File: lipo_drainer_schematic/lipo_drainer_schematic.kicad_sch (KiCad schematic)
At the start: 55 parts, among them J1 BATT, J2 FAN, J3 Vcal, J4 128x64_OLED, J5 Gcal, J6 Ical, Q1 MMBT3904, Q10 FQP27P06, Q11 FQP27P06, Q2 IRLML5103TRPBF, Q5 IRLML5103TRPBF, Q6 MMBT3904, Q7 FQP27P06, Q8 FQP27P06, Q9 MMBT3904, SW1 BT1, SW2 BT2, SW3 BT3, SW4 BT4, SW5 ON, SW6 RUN, U1 LM2936-3.3_TO92, U2 Pico, U4 LM4040DBZ-3, U5 LM4040DBZ-3

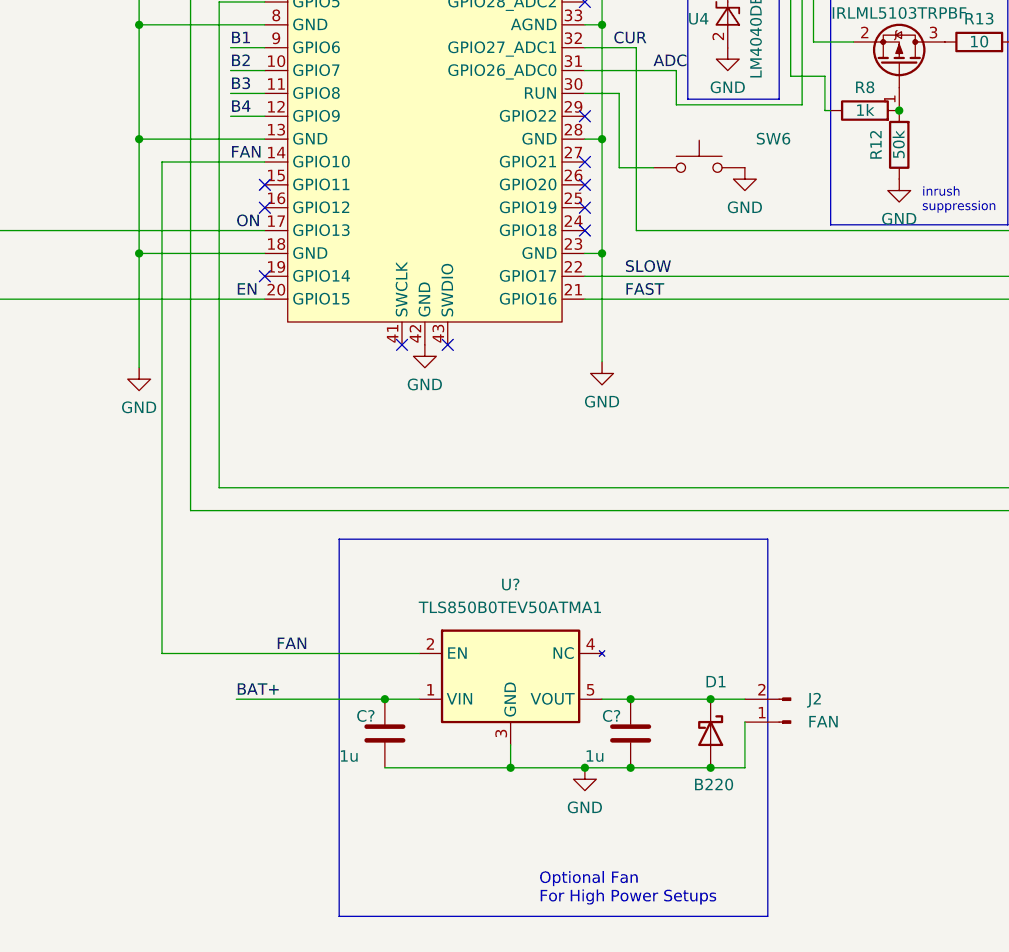
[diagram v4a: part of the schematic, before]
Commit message: Adding more to the README
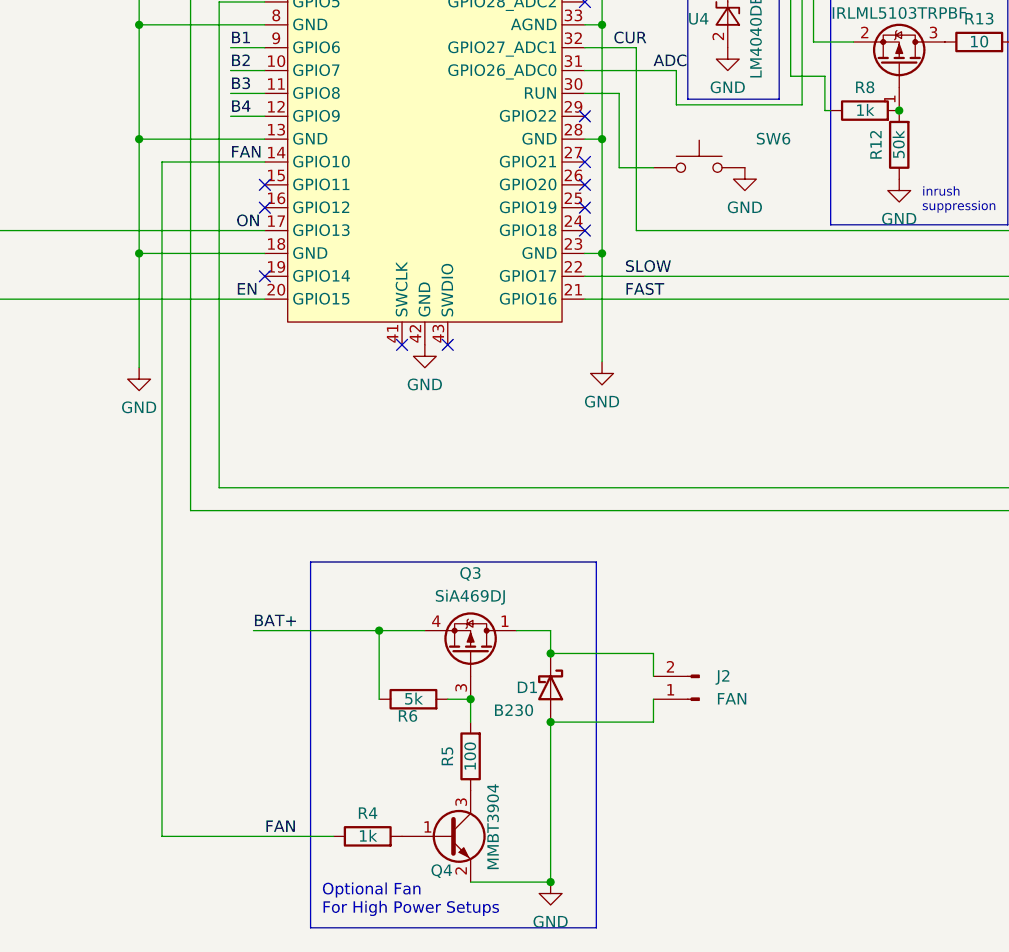
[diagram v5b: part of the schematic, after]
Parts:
- removed C? (x2): 1u, symbol Device:C
- removed U?: TLS850B0TEV50ATMA1, Package_TO_SOT_SMD:TO-252-5_TabPin3, symbol Regulator_Linear:MIC29152WU
- added Q3: SiA469DJ, Package_TO_SOT_SMD:Vishay_PowerPAK_SC70-6L_Single, symbol Transistor_FET:SiA449DJ
- added Q4: MMBT3904, Package_TO_SOT_SMD:SOT-23, symbol Transistor_BJT:MMBT3904
- added R4: 1k, Resistor_SMD:R_0805_2012Metric_Pad1.20x1.40mm_HandSolder, symbol Device:R
- added R5: 100, Resistor_SMD:R_0805_2012Metric_Pad1.20x1.40mm_HandSolder, symbol Device:R
- added R6: 5k, Resistor_SMD:R_0805_2012Metric_Pad1.20x1.40mm_HandSolder, symbol Device:R
- D1: value B220 -> B230
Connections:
- net BAT+: now also Q3.4 (S), R6.1
- net FAN: now also R4.1
- net GND: now also Q4.2 (E)
- net at D1.1 (K), J2.2 (Pin_2): now also Q3.1 (D)
- new net: Q4.3 (C), R5.1
- new net: Q3.3 (G), R5.2, R6.2
- new net: Q4.1 (B), R4.2
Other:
- moved on the sheet: D1, J2

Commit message: more README work
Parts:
- removed U1: LM2936-3.3_TO92, Package_TO_SOT_THT:TO-92_Inline, symbol Regulator_Linear:LM2936-3.3_TO92
- added U3: TPS70933DBVR, Package_TO_SOT_SMD:SOT-23-5, symbol Regulator_Linear:TPS7A0508PDBV
- F1: value Fuse -> MHP-TAT18-9-90N; footprint (none) -> Fuse:Fuse_Schurter_UMZ250
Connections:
- net 3.3V: now also U3.5 (OUT)
- net BAT+: now also F1.1; no longer Q10.3 (S), Q11.3 (S), Q7.3 (S), Q8.3 (S), R16.1
- net GND: now also U3.2 (GND)
- net at Q10.2 (D), Q11.2 (D), Q7.2 (D)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: now also J6.2 (Pin_2), R21.2, R22.2, R23.2, R24.2; no longer F1.2
- net at C1.1, J3.2 (Pin_2), Q2.3 (D)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: now also U3.1 (IN)
- new net: F1.2, Q10.3 (S), Q11.3 (S), Q7.3 (S), Q8.3 (S), R16.1
- no-connect marks 17 -> 18
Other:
- moved on the sheet: F1

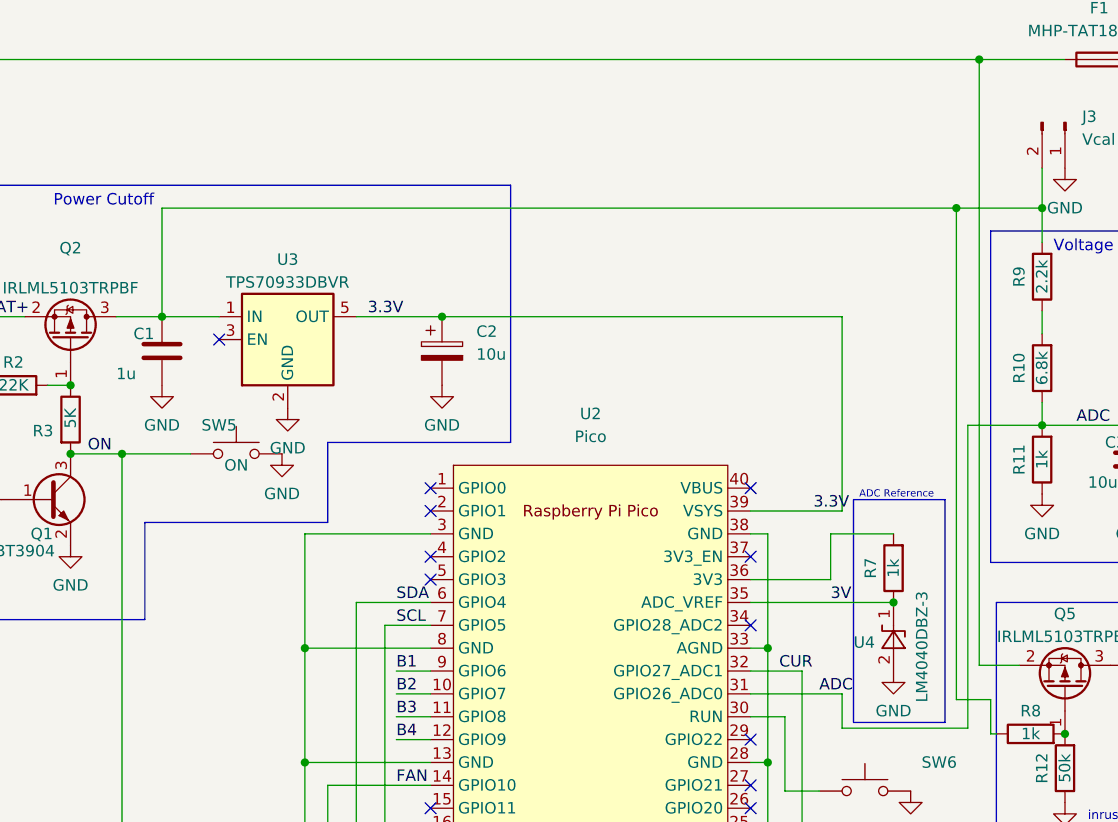
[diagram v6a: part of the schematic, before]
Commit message: Fixed ERC warnings
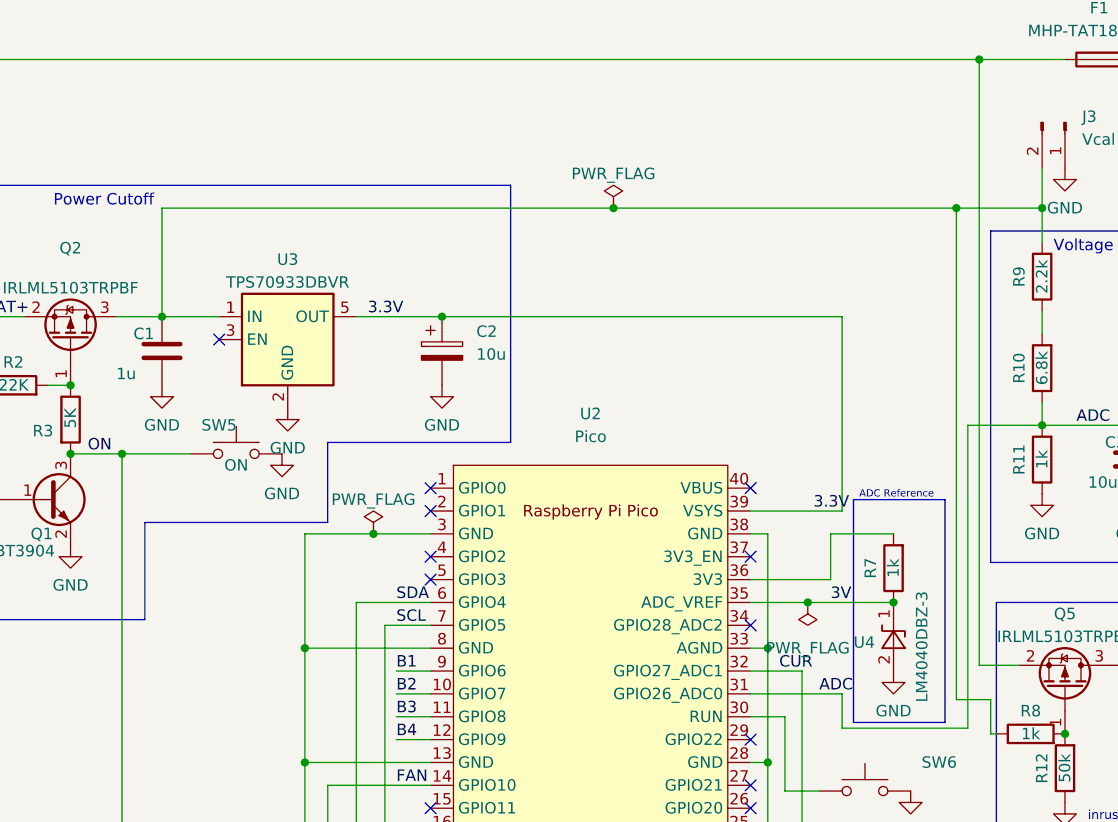
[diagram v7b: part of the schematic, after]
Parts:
- J1: symbol Connector:Conn_01x02_Female -> Connector:Conn_01x02_Socket
- J2, J3, J5, J6: symbol Connector:Conn_01x02_Male -> Connector:Conn_01x02_Pin
- J4: symbol Connector:Conn_01x04_Male -> Connector:Conn_01x04_Pin
- U2: footprint Raspberry_Pi_Pico:RPi_Pico_SMD_TH -> RPi_Pico:RPi_Pico_SMD_TH; symbol PI PICO:Pico -> MCU_RaspberryPi_and_Boards:Pico
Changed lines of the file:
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@@
   (junction (at 256.54 90.805) (diameter 0) (color 0 0 0 0)
   )
+  (junction (at 100.33 80.01) (diameter 0) (color 0 0 0 0)
+  )
   (junction (at 165.1 43.815) (diameter 0) (color 0 0 0 0)
   )
@@
   (junction (at 119.38 160.02) (diameter 0) (color 0 0 0 0)
   )
+  (junction (at 148.59 87.63) (diameter 0) (color 0 0 0 0)
+  )
   (junction (at 92.71 118.11) (diameter 0) (color 0 0 0 0)
   )
@@
   )
   (junction (at 258.445 59.055) (diameter 0) (color 0 0 0 0)
+  )
+  (junction (at 127 43.815) (diameter 0) (color 0 0 0 0)
   )
   (junction (at 92.71 105.41) (diameter 0) (color 0 0 0 0)
@@
     (stroke (width 0) (type default))
   )
+  (wire (pts (xy 100.33 80.01) (xy 92.71 80.01))
+    (stroke (width 0) (type default))
+  )
   (wire (pts (xy 101.6 90.17) (xy 106.68 90.17))
     (stroke (width 0) (type default))
@@
     (stroke (width 0) (type default))
   )
+  (wire (pts (xy 29.21 27.305) (xy 56.515 27.305))
+    (stroke (width 0) (type default))
+  )
+  (wire (pts (xy 127 43.815) (xy 165.1 43.815))
+    (stroke (width 0) (type default))
+  )
   (wire (pts (xy 138.43 160.02) (xy 138.43 162.56))
     (stroke (width 0) (type default))
@@
     (stroke (width 0) (type default))
   )
-  (wire (pts (xy 106.68 80.01) (xy 92.71 80.01))
+  (wire (pts (xy 106.68 80.01) (xy 100.33 80.01))
     (stroke (width 0) (type default))
   )
@@
     (stroke (width 0) (type default))
   )
+  (wire (pts (xy 148.59 87.63) (xy 158.115 87.63))
+    (stroke (width 0) (type default))
+  )
   (wire (pts (xy 223.52 86.995) (xy 238.76 86.995))
     (stroke (width 0) (type default))
@@
     (stroke (width 0) (type default))
   )
-  (wire (pts (xy 76.835 43.815) (xy 165.1 43.815))
+  (wire (pts (xy 76.835 43.815) (xy 127 43.815))
     (stroke (width 0) (type default))
   )
@@
     (stroke (width 0) (type default))
   )
-  (wire (pts (xy 142.24 87.63) (xy 158.115 87.63))
+  (wire (pts (xy 142.24 87.63) (xy 148.59 87.63))
     (stroke (width 0) (type default))
   )
@@
   )
   (wire (pts (xy 129.54 167.64) (xy 129.54 170.18))
-    (stroke (width 0) (type default))
-  )
-  (wire (pts (xy 29.21 27.305) (xy 56.515 27.305))
     (stroke (width 0) (type default))
   )
@@
     )
   )
-  (symbol (lib_id "Connector:Conn_01x02_Female") (at 24.13 29.845 180) (unit 1)
+  (symbol (lib_id "Connector:Conn_01x02_Socket") (at 24.13 29.845 180) (unit 1)
     (in_bom yes) (on_board yes) (dnp no)
     (property "Reference" "J1" (at 19.685 30.48 90)
@@
     )
   )
-  (symbol (lib_id "Connector:Conn_01x02_Male") (at 177.165 34.29 270) (unit 1)
+  (symbol (lib_id "Connector:Conn_01x02_Pin") (at 177.165 34.29 270) (unit 1)
     (in_bom yes) (on_board yes) (dnp no) (fields_autoplaced)
     (property "Reference" "J3" (at 179.07 33.6549 90)
@@
     )
   )
+  (symbol (lib_id "power:PWR_FLAG") (at 148.59 87.63 180) (unit 1)
+    (in_bom yes) (on_board yes) (dnp no) (fields_autoplaced)
+    (property "Reference" "#FLG02" (at 148.59 89.535 0)
+      (effects (font (size 1.27 1.27)) hide)
+    )
+    (property "Value" "PWR_FLAG" (at 148.59 92.71 0)
+      (effects (font (size 1.27 1.27)))
+    )
+    (property "Footprint" "" (at 148.59 87.63 0)
+      (effects (font (size 1.27 1.27)) hide)
+    )
+    (property "Datasheet" "~" (at 148.59 87.63 0)
+      (effects (font (size 1.27 1.27)) hide)
+    )
+    (pin "1")
+    (instances
+      (project "lipo_drainer_schematic"
+        (path "/db6692d0-0595-40e8-a350-9f6ef4d6e67d"
+          (reference "#FLG02") (unit 1)
+        )
+      )
+    )
+  )
   (symbol (lib_id "Transistor_FET:FQP27P06") (at 225.425 50.8 270) (mirror x) (unit 1)
     (in_bom yes) (on_board yes) (dnp no) (fields_autoplaced)
@@
     )
   )
+  (symbol (lib_id "power:PWR_FLAG") (at 127 43.815 0) (unit 1)
+    (in_bom yes) (on_board yes) (dnp no) (fields_autoplaced)
+    (property "Reference" "#FLG03" (at 127 41.91 0)
+      (effects (font (size 1.27 1.27)) hide)
+    )
+    (property "Value" "PWR_FLAG" (at 127 40.005 0)
+      (effects (font (size 1.27 1.27)))
+    )
+    (property "Footprint" "" (at 127 43.815 0)
+      (effects (font (size 1.27 1.27)) hide)
+    )
+    (property "Datasheet" "~" (at 127 43.815 0)
+      (effects (font (size 1.27 1.27)) hide)
+    )
+    (pin "1")
+    (instances
+      (project "lipo_drainer_schematic"
+        (path "/db6692d0-0595-40e8-a350-9f6ef4d6e67d"
+          (reference "#FLG03") (unit 1)
+        )
+      )
+    )
+  )
   (symbol (lib_id "Device:C") (at 184.785 71.755 0) (unit 1)
     (in_bom yes) (on_board yes) (dnp no)
@@
     )
   )
-  (symbol (lib_id "Connector:Conn_01x02_Male") (at 278.13 79.375 270) (unit 1)
+  (symbol (lib_id "Connector:Conn_01x02_Pin") (at 278.13 79.375 270) (unit 1)
     (in_bom yes) (on_board yes) (dnp no) (fields_autoplaced)
     (property "Reference" "J6" (at 279.4 78.7399 90)
@@
     )
   )
-  (symbol (lib_id "Connector:Conn_01x04_Male") (at 227.965 137.795 0) (mirror y) (unit 1)
+  (symbol (lib_id "Connector:Conn_01x04_Pin") (at 227.965 137.795 0) (mirror y) (unit 1)
     (in_bom yes) (on_board yes) (dnp no) (fields_autoplaced)
     (property "Reference" "J4" (at 229.87 137.7949 0)
@@
     )
   )
+  (symbol (lib_id "power:PWR_FLAG") (at 100.33 80.01 0) (unit 1)
+    (in_bom yes) (on_board yes) (dnp no) (fields_autoplaced)
+    (property "Reference" "#FLG01" (at 100.33 78.105 0)
+      (effects (font (size 1.27 1.27)) hide)
+    )
+    (property "Value" "PWR_FLAG" (at 100.33 76.2 0)
+      (effects (font (size 1.27 1.27)))
+    )
+    (property "Footprint" "" (at 100.33 80.01 0)
+      (effects (font (size 1.27 1.27)) hide)
+    )
+    (property "Datasheet" "~" (at 100.33 80.01 0)
+      (effects (font (size 1.27 1.27)) hide)
+    )
+    (pin "1")
+    (instances
+      (project "lipo_drainer_schematic"
+        (path "/db6692d0-0595-40e8-a350-9f6ef4d6e67d"
+          (reference "#FLG01") (unit 1)
+        )
+      )
+    )
+  )
   (symbol (lib_id "Switch:SW_Push") (at 85.09 71.12 0) (unit 1)
     (in_bom yes) (on_board yes) (dnp no)
@@
     )
   )
-  (symbol (lib_id "Connector:Conn_01x02_Male") (at 154.94 167.64 180) (unit 1)
+  (symbol (lib_id "Connector:Conn_01x02_Pin") (at 154.94 167.64 180) (unit 1)
     (in_bom yes) (on_board yes) (dnp no)
     (property "Reference" "J2" (at 156.845 165.0999 0)
@@
     )
   )
-  (symbol (lib_id "PI PICO:Pico") (at 124.46 99.06 0) (unit 1)
+  (symbol (lib_id "MCU_RaspberryPi_and_Boards:Pico") (at 124.46 99.06 0) (unit 1)
     (in_bom yes) (on_board yes) (dnp no) (fields_autoplaced)
     (property "Reference" "U2" (at 124.46 66.675 0)
@@
       (effects (font (size 1.27 1.27)))
     )
-    (property "Footprint" "Raspberry_Pi_Pico:RPi_Pico_SMD_TH" (at 124.46 99.06 90)
+    (property "Footprint" "RPi_Pico:RPi_Pico_SMD_TH" (at 124.46 99.06 90)
       (effects (font (size 1.27 1.27)) hide)
     )
@@
     )
   )
+  (symbol (lib_id "power:GND") (at 184.785 75.565 0) (unit 1)
+    (in_bom yes) (on_board yes) (dnp no) (fields_autoplaced)
+    (property "Reference" "#PWR012" (at 184.785 81.915 0)
+      (effects (font (size 1.27 1.27)) hide)
+    )
+    (property "Value" "GND" (at 184.785 80.01 0)
+      (effects (font (size 1.27 1.27)))
+    )
+    (property "Footprint" "" (at 184.785 75.565 0)
+      (effects (font (size 1.27 1.27)) hide)
+    )
+    (property "Datasheet" "" (at 184.785 75.565 0)
+      (effects (font (size 1.27 1.27)) hide)
+    )
+    (pin "1")
+    (instances
+      (project "lipo_drainer_schematic"
+        (path "/db6692d0-0595-40e8-a350-9f6ef4d6e67d"
+          (reference "#PWR012") (unit 1)
+        )
+      )
+    )
+  )
   (symbol (lib_id "Device:R") (at 177.165 106.045 180) (unit 1)
     (in_bom yes) (on_board yes) (dnp no)
@@
     )
   )
-  (symbol (lib_id "Connector:Conn_01x02_Male") (at 268.605 56.515 270) (unit 1)
+  (symbol (lib_id "Connector:Conn_01x02_Pin") (at 268.605 56.515 270) (unit 1)
     (in_bom yes) (on_board yes) (dnp no) (fields_autoplaced)
     (property "Reference" "J5" (at 270.51 55.8799 90)
@@
         )
       )
-    )
-  )
-  (symbol (lib_id "power:GND") (at 184.785 75.565 0) (unit 1)
-    (in_bom yes) (on_board yes) (dnp no) (fields_autoplaced)
-    (property "Reference" "#PWR018" (at 184.785 81.915 0)
-      (effects (font (size 1.27 1.27)) hide)
-    )
-    (property "Value" "GND" (at 184.785 80.01 0)
-      (effects (font (size 1.27 1.27)))
-    )
-    (property "Footprint" "" (at 184.785 75.565 0)
-      (effects (font (size 1.27 1.27)) hide)
-    )
-    (property "Datasheet" "" (at 184.785 75.565 0)
-      (effects (font (size 1.27 1.27)) hide)
-    )
-    (pin "1")
-    (instances
-      (project "lipo_drainer_schematic"
-        (path "/db6692d0-0595-40e8-a350-9f6ef4d6e67d"
-          (reference "#PWR018") (unit 1)
-        )
-      )

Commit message: Added parts list
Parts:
- C1, C2, C3, C4: footprint (none) -> Capacitor_SMD:C_1206_3216Metric_Pad1.33x1.80mm_HandSolder
- Q10, Q11, Q7, Q8: value FQP27P06 -> G700P06T
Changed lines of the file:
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@@
       (effects (font (size 1.27 1.27)))
     )
-    (property "Value" "FQP27P06" (at 212.725 54.61 90)
+    (property "Value" "G700P06T" (at 212.725 54.61 90)
       (effects (font (size 1.27 1.27)))
     )
@@
       (effects (font (size 1.27 1.27)) (justify left))
     )
-    (property "Footprint" "" (at 108.9152 63.5 0)
+    (property "Footprint" "Capacitor_SMD:C_1206_3216Metric_Pad1.33x1.80mm_HandSolder" (at 108.9152 63.5 0)
       (effects (font (size 1.27 1.27)) hide)
     )
@@
       (effects (font (size 1.27 1.27)))
     )
-    (property "Value" "FQP27P06" (at 225.425 43.815 90)
+    (property "Value" "G700P06T" (at 225.425 43.815 90)
       (effects (font (size 1.27 1.27)))
     )
@@
       (effects (font (size 1.27 1.27)))
     )
-    (property "Value" "FQP27P06" (at 253.365 22.86 90)
+    (property "Value" "G700P06T" (at 253.365 22.86 90)
       (effects (font (size 1.27 1.27)))
     )
@@
       (effects (font (size 1.27 1.27)))
     )
-    (property "Value" "FQP27P06" (at 238.76 33.655 90)
+    (property "Value" "G700P06T" (at 238.76 33.655 90)
       (effects (font (size 1.27 1.27)))
     )
@@
       (effects (font (size 1.27 1.27)) (justify left))
     )
-    (property "Footprint" "" (at 185.7502 75.565 0)
+    (property "Footprint" "Capacitor_SMD:C_1206_3216Metric_Pad1.33x1.80mm_HandSolder" (at 185.7502 75.565 0)
       (effects (font (size 1.27 1.27)) hide)
     )
@@
       (effects (font (size 1.27 1.27)) (justify left))
     )
-    (property "Footprint" "" (at 77.8002 63.5 0)
+    (property "Footprint" "Capacitor_SMD:C_1206_3216Metric_Pad1.33x1.80mm_HandSolder" (at 77.8002 63.5 0)
       (effects (font (size 1.27 1.27)) hide)
     )
@@
       (effects (font (size 1.27 1.27)) (justify left))
     )
-    (property "Footprint" "" (at 247.9802 74.295 0)
-      (effects (font (size 1.27 1.27)) hide)
-    )
+    (property "Footprint" "Capacitor_SMD:C_1206_3216Metric_Pad1.33x1.80mm_HandSolder" (at 247.9802 74.295 0)
+      (effects (font (size 1.27 1.27)) hide)
+    )
